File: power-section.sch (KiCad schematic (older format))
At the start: 6 parts, among them U1 LM2574M-3.3

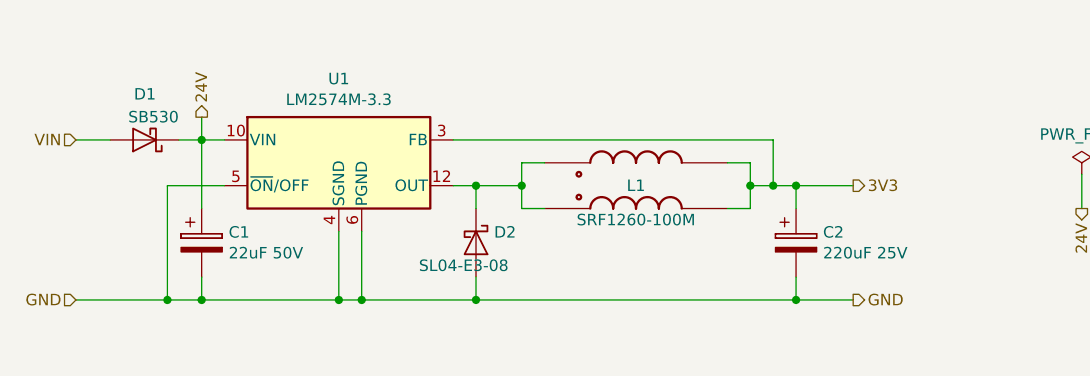
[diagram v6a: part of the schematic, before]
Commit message: Changed Motor Controller to DRV8840, removed pre-motor power section. Replaced PNP transistors in logic level shifters with P-MOSFET units
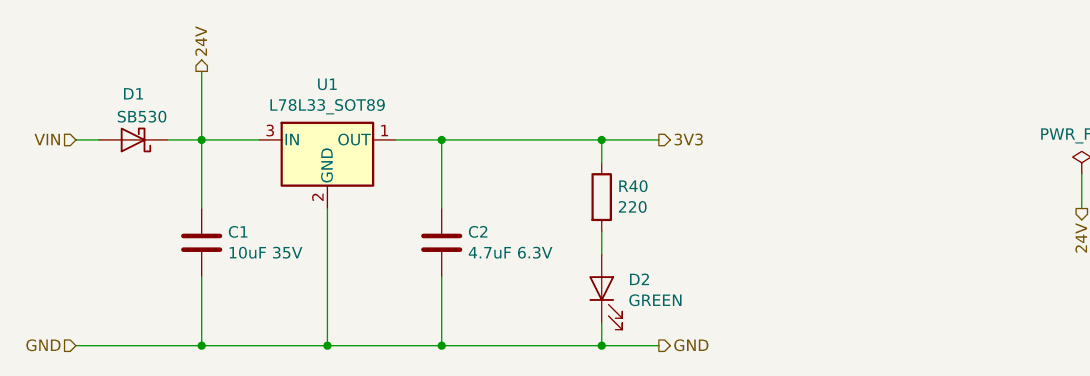
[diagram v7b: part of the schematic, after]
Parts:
- removed C1: 22uF 50V, Capacitor_SMD:CP_Elec_5x5.8, symbol Device:CP
- removed C2: 220uF 25V, Capacitor_THT:CP_Radial_D6.3mm_P2.50mm, symbol Device:CP
- removed D2: SL04-E3-08, Diode_SMD:D_SOD-123F, symbol Device:D_Schottky
- removed L1: SRF1260-100M, SRF1260-100M:IND_SRF1260-100M, symbol SRF1260-100M:SRF1260-100M
- removed U1: LM2574M-3.3, Package_SO:SOIC-14W_7.5x9.0mm_P1.27mm, symbol Regulator_Switching:LM2574M-3.3
- added C1: 10uF 35V, Capacitor_SMD:C_1210_3225Metric_Pad1.42x2.65mm_HandSolder, symbol Device:C
- added C2: 4.7uF 6.3V, Capacitor_SMD:C_0805_2012Metric_Pad1.15x1.40mm_HandSolder, symbol Device:C
- added D2: GREEN, LED_SMD:LED_0603_1608Metric_Castellated, symbol Device:LED
- added R40: 220, Resistor_SMD:R_0603_1608Metric, symbol Device:R
- added U1: L78L33_SOT89, Package_TO_SOT_SMD:SOT-89-3_Handsoldering, symbol Regulator_Linear:L78L33_SOT89
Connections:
- net 24V: now also C1.1, U1.3 (IN)
- net 3V3: now also C2.1, R40.1, U1.1 (OUT)
- net GND: now also C1.2, C2.2, D2.1 (K), U1.2 (GND)
- new net: D2.2 (A), R40.2
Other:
- moved on the sheet: D1
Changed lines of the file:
@@
 $Descr A4 11693 8268
 encoding utf-8
-Sheet 2 10
+Sheet 2 8
 Title ""
 Date ""
@@
 Comment4 ""
 $EndDescr
-Text HLabel 7950 2050 2    50   Output ~ 0
+Text HLabel 7100 1850 2    50   Output ~ 0
 3V3
 Wire Wire Line
-	4550 1850 4700 1850
-Text HLabel 7950 2550 2    50   Output ~ 0
+	4550 1850 4650 1850
+Text HLabel 7100 2750 2    50   Output ~ 0
 GND
-Text HLabel 4550 2550 0    50   Input ~ 0
+Text HLabel 4550 2750 0    50   Input ~ 0
 GND
 Text HLabel 4550 1850 0    50   Input ~ 0
 VIN
-Text HLabel 5100 1750 1    50   Output ~ 0
+Text HLabel 5100 1550 1    50   Output ~ 0
 24V
 $Comp
 L Device:D_Schottky D1
 U 1 1 5BE562E4
-P 4850 1850
+P 4800 1850
 AR Path="/5BDAF501/5BE562E4" Ref="D1"  Part="1"
 AR Path="/5BE562E4" Ref="D?"  Part="1"
-F 0 "D1" H 4800 1650 50  0000 L CNN
-F 1 "SB530" H 4700 1750 50  0000 L CNN
-F 2 "PTVS3V3P1UP:SOD128" H 4850 1850 50  0001 C CNN
-F 3 "~" H 4850 1850 50  0001 C CNN
-	1    4850 1850
+F 0 "D1" H 4750 1650 50  0000 L CNN
+F 1 "SB530" H 4650 1750 50  0000 L CNN
+F 2 "PTVS3V3P1UP:SOD128" H 4800 1850 50  0001 C CNN
+F 3 "~" H 4800 1850 50  0001 C CNN
+	1    4800 1850
 	-1   0    0    1
 $EndComp
@@
 Wire Wire Line
 	8950 2150 8950 2000
+Wire Wire Line
+	4950 1850 5100 1850
+Connection ~ 5100 1850
+Wire Wire Line
+	5100 1850 5350 1850
+Wire Wire Line
+	5100 1850 5100 1550
+Wire Wire Line
+	5100 2450 5100 2750
 $Comp
-L Regulator_Switching:LM2574M-3.3 U1
-U 1 1 5BE562F3
-P 5700 1950
-F 0 "U1" H 5700 2317 50  0000 C CNN
-F 1 "LM2574M-3.3" H 5700 2226 50  0000 C CNN
-F 2 "Package_SO:SOIC-14W_7.5x9.0mm_P1.27mm" H 5300 2300 50  0001 L CIN
-F 3 "http://www.national.com/ds/LM/LM2574.pdf" H 5700 1950 50  0001 C CNN
-	1    5700 1950
+L Regulator_Linear:L78L33_SOT89 U1
+U 1 1 5BF1ED5D
+P 5650 1850
+F 0 "U1" H 5650 2092 50  0000 C CNN
+F 1 "L78L33_SOT89" H 5650 2001 50  0000 C CNN
+F 2 "Package_TO_SOT_SMD:SOT-89-3_Handsoldering" H 5650 2050 50  0001 C CIN
+F 3 "http://www.st.com/content/ccc/resource/technical/document/datasheet/15/55/e5/aa/23/5b/43/fd/CD00000446.pdf/files/CD00000446.pdf/jcr:content/translations/en.CD00000446.pdf" H 5650 1800 50  0001 C CNN
+	1    5650 1850
 	1    0    0    -1
 $EndComp
 Wire Wire Line
-	5000 1850 5100 1850
+	4550 2750 5100 2750
 $Comp
-L Device:CP C1
-U 1 1 5BE562FB
+L Device:C C1
+U 1 1 5BF1EFF2
 P 5100 2300
-F 0 "C1" H 5218 2346 50  0000 L CNN
-F 1 "22uF 50V" H 5218 2255 50  0000 L CNN
-F 2 "Capacitor_SMD:CP_Elec_5x5.8" H 5138 2150 50  0001 C CNN
+F 0 "C1" H 5215 2346 50  0000 L CNN
+F 1 "10uF 35V" H 5215 2255 50  0000 L CNN
+F 2 "Capacitor_SMD:C_1210_3225Metric_Pad1.42x2.65mm_HandSolder" H 5138 2150 50  0001 C CNN
 F 3 "~" H 5100 2300 50  0001 C CNN
 	1    5100 2300
 	1    0    0    -1
 $EndComp
-Wire Wire Line
-	5100 2150 5100 1850
-Connection ~ 5100 1850
-Wire Wire Line
-	5100 1850 5200 1850
-Wire Wire Line
-	4550 2550 4950 2550
-Wire Wire Line
-	5800 2550 5800 2250
-Wire Wire Line
-	5100 2450 5100 2550
-Connection ~ 5100 2550
-Wire Wire Line
-	5100 2550 5700 2550
-Wire Wire Line
-	5700 2250 5700 2550
-Connection ~ 5700 2550
-Wire Wire Line
-	5700 2550 5800 2550
-Wire Wire Line
-	5200 2050 4950 2050
-Wire Wire Line
-	4950 2050 4950 2550
-Connection ~ 4950 2550
-Wire Wire Line
-	4950 2550 5100 2550
 $Comp
-L Device:D_Schottky D2
-U 1 1 5BE56311
-P 6300 2300
-F 0 "D2" V 6254 2379 50  0000 L CNN
-F 1 "SL04-E3-08" V 6400 2050 50  0000 L CNN
-F 2 "Diode_SMD:D_SOD-123F" H 6300 2300 50  0001 C CNN
-F 3 "~" H 6300 2300 50  0001 C CNN
-	1    6300 2300
-	0    1    1    0
-$EndComp
-Wire Wire Line
-	6200 2050 6300 2050
-Wire Wire Line
-	6300 2050 6300 2150
-Wire Wire Line
-	5800 2550 6300 2550
-Wire Wire Line
-	6300 2550 6300 2450
-Connection ~ 5800 2550
-$Comp
-L Device:CP C2
-U 1 1 5BE5631D
-P 7700 2300
-F 0 "C2" H 7818 2346 50  0000 L CNN
-F 1 "220uF 25V" H 7818 2255 50  0000 L CNN
-F 2 "Capacitor_THT:CP_Radial_D6.3mm_P2.50mm" H 7738 2150 50  0001 C CNN
-F 3 "~" H 7700 2300 50  0001 C CNN
-	1    7700 2300
+L Device:C C2
+U 1 1 5BF1F211
+P 6150 2300
+F 0 "C2" H 6265 2346 50  0000 L CNN
+F 1 "4.7uF 6.3V" H 6265 2255 50  0000 L CNN
+F 2 "Capacitor_SMD:C_0805_2012Metric_Pad1.15x1.40mm_HandSolder" H 6188 2150 50  0001 C CNN
+F 3 "~" H 6150 2300 50  0001 C CNN
+	1    6150 2300
 	1    0    0    -1
 $EndComp
 Wire Wire Line
-	7700 2550 7700 2450
-Connection ~ 6300 2050
+	6150 2750 6150 2450
 Wire Wire Line
-	7700 2150 7700 2050
-Connection ~ 7700 2050
+	6150 2750 6850 2750
+Connection ~ 6150 2750
 Wire Wire Line
-	7950 2050 7700 2050
+	6150 1850 5950 1850
 Wire Wire Line
-	5100 1850 5100 1750
-Wire Wire Line
-	7600 2050 7700 2050
-Connection ~ 7700 2550
-Wire Wire Line
-	7950 2550 7700 2550
-Wire Wire Line
-	6500 2050 6500 1950
-Wire Wire Line
-	6500 1950 6600 1950
-Wire Wire Line
-	6300 2050 6500 2050
-Wire Wire Line
-	6500 2050 6500 2150
-Wire Wire Line
-	6500 2150 6600 2150
-Connection ~ 6500 2050
-Wire Wire Line
-	7400 1950 7500 1950
-Wire Wire Line
-	7500 1950 7500 2050
-Wire Wire Line
-	7500 2150 7400 2150
-Wire Wire Line
-	7600 1850 7600 2050
-Wire Wire Line
-	7600 2050 7500 2050
-Connection ~ 7500 2050
-Wire Wire Line
-	7500 2050 7500 2150
-Connection ~ 7600 2050
+	6150 1850 6850 1850
+Connection ~ 6150 1850
 $Comp
-L SRF1260-100M:SRF1260-100M L1
-U 1 1 5BE5EC2D
-P 7000 2050
-F 0 "L1" H 7000 2050 50  0000 C CNN
-F 1 "SRF1260-100M" H 7000 1900 50  0000 C CNN
-F 2 "SRF1260-100M:IND_SRF1260-100M" H 7000 2050 50  0001 L BNN
-F 3 "Inductor Power Shielded Wirewound 10uH/40uH 20% 100KHz Ferrite 5.35A/2.67A 24.6mOhm/93.4mOhm DCR T/R" H 7000 2050 50  0001 L BNN
-F 4 "Bourns" H 7000 2050 50  0001 L BNN "Field4"
-F 5 "Nonstandard Bourns" H 7000 2050 50  0001 L BNN "Field5"
-F 6 "SRF1260-100M" H 7000 2050 50  0001 L BNN "Field6"
-F 7 "None" H 7000 2050 50  0001 L BNN "Field7"
-F 8 "Unavailable" H 7000 2050 50  0001 L BNN "Field8"
-	1    7000 2050
+L Device:LED D2
+U 1 1 5BF1F6EB
+P 6850 2500
+F 0 "D2" V 6888 2383 50  0000 R CNN
+F 1 "GREEN" V 6797 2383 50  0000 R CNN
+F 2 "LED_SMD:LED_0603_1608Metric_Castellated" H 6850 2500 50  0001 C CNN
+F 3 "~" H 6850 2500 50  0001 C CNN
+	1    6850 2500
+	0    -1   -1   0
+$EndComp
+$Comp
+L Device:R R40
+U 1 1 5BF1FB5D
+P 6850 2100
+F 0 "R40" H 6920 2146 50  0000 L CNN
+F 1 "220" H 6920 2055 50  0000 L CNN
+F 2 "Resistor_SMD:R_0603_1608Metric" V 6780 2100 50  0001 C CNN
+F 3 "~" H 6850 2100 50  0001 C CNN
+	1    6850 2100
 	1    0    0    -1
 $EndComp
 Wire Wire Line
-	6300 2550 7700 2550
-Connection ~ 6300 2550
+	6850 1950 6850 1850
+Connection ~ 6850 1850
 Wire Wire Line
-	6200 1850 7600 1850
+	6850 1850 7100 1850
+Wire Wire Line
+	6850 2250 6850 2350
+Wire Wire Line
+	5100 2750 5650 2750
+Connection ~ 5100 2750
+Wire Wire Line
+	5650 2150 5650 2750
+Connection ~ 5650 2750
+Wire Wire Line
+	5650 2750 6150 2750
+Wire Wire Line
+	6150 1850 6150 2150
+Wire Wire Line
+	5100 1850 5100 2150
+Wire Wire Line
+	6850 2650 6850 2750
+Connection ~ 6850 2750
+Wire Wire Line
+	6850 2750 7100 2750
 $EndSCHEMATC

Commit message: Re-placed components of 3.3->24V converter. Improvement placement of Motor Controller components
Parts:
- D1: footprint PTVS3V3P1UP:SOD128 -> Diode_THT:D_DO-201AD_P3.81mm_Vertical_KathodeUp
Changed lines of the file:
@@
 F 0 "D1" H 4750 1650 50  0000 L CNN
 F 1 "SB530" H 4650 1750 50  0000 L CNN
-F 2 "PTVS3V3P1UP:SOD128" H 4800 1850 50  0001 C CNN
+F 2 "Diode_THT:D_DO-201AD_P3.81mm_Vertical_KathodeUp" H 4800 1850 50  0001 C CNN
 F 3 "~" H 4800 1850 50  0001 C CNN
 	1    4800 1850
